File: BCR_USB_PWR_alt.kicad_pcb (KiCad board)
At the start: 2 copper layers, 32.2 x 17 mm, 2 parts, among them CN1 DB9_Female, CN2 UE27AC54100

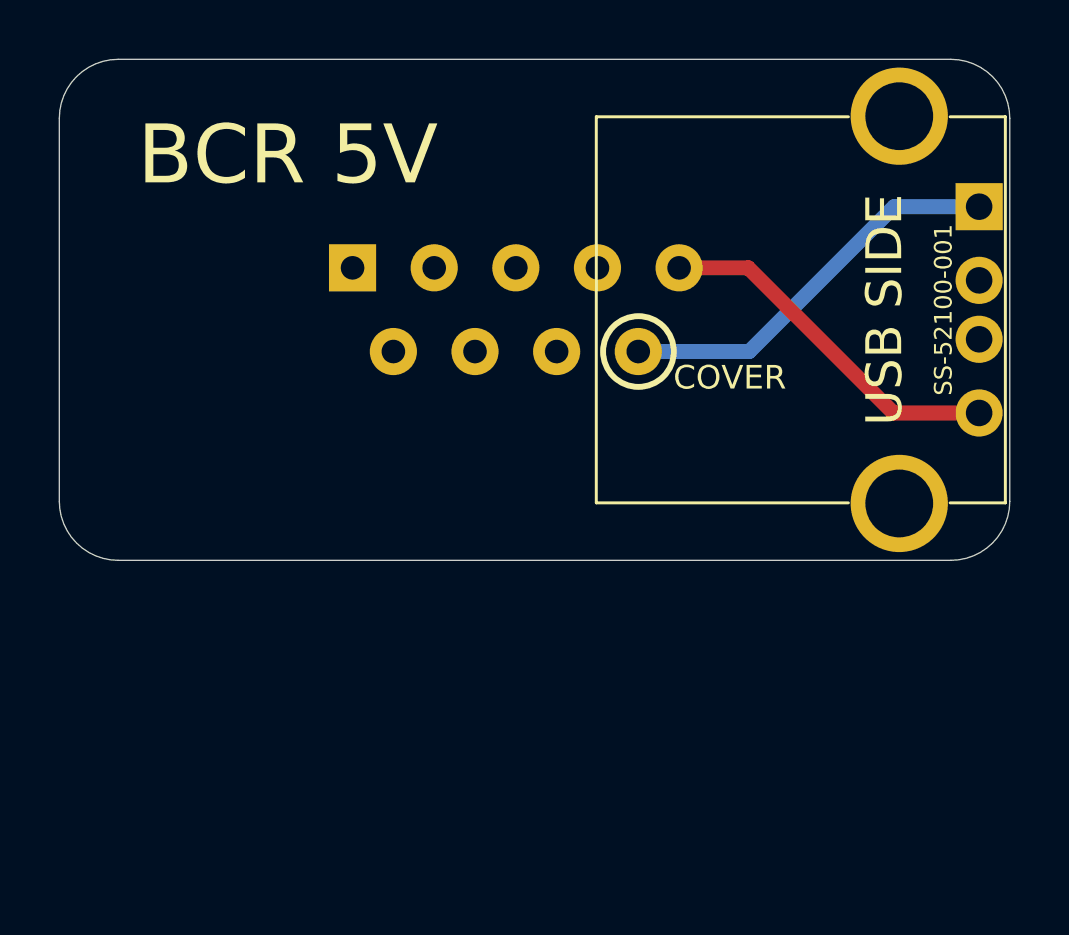
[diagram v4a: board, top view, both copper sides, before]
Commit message: db9 pin 7 is the real GND, not pin 5
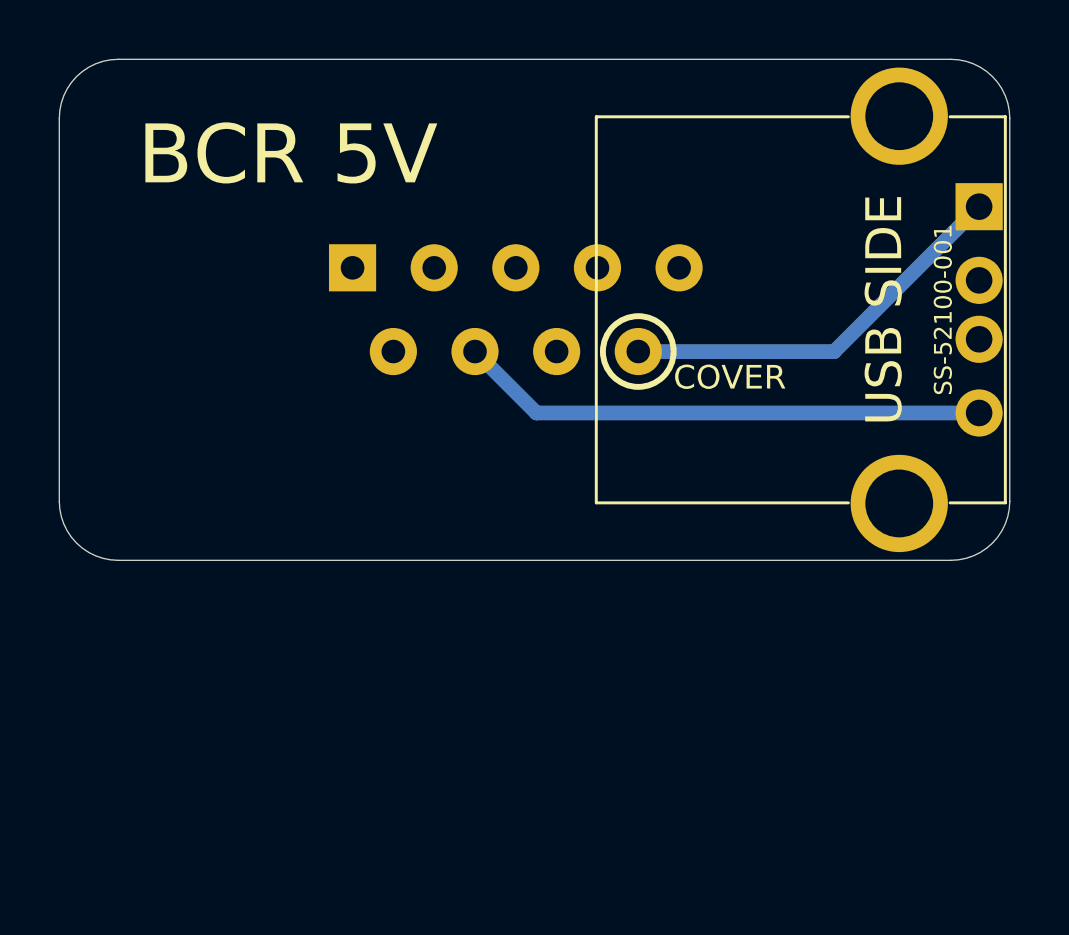
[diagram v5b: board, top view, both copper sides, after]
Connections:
- CN1 pad 5: /GND -> (no net)
- CN1 pad 7: (no net) -> /GND
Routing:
- net /GND: track 12.2 -> 18.0 mm
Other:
- net class Default: clearance 0.2 -> 0.16; trace_width 0.25 -> 0.16; via_dia 0.8 -> 0.42; via_drill 0.4 -> 0.26
- rule trace_clearance: 0.2 -> 0.16
- rule trace_min: 0.2 -> 0.16
- rule via_min_drill: 0.3 -> 0.26
- rule via_min_size: 0.4 -> 0.42
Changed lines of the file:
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@@
     (thickness 1.6)
     (drawings 23)
-    (tracks 6)
+    (tracks 4)
     (zones 0)
     (modules 2)
@@
   )
   (setup
-    (last_trace_width 0.25)
-    (user_trace_width 0.508)
-    (trace_clearance 0.2)
+    (last_trace_width 0.16)
+    (user_trace_width 0.5)
+    (trace_clearance 0.16)
     (zone_clearance 0.508)
     (zone_45_only no)
-    (trace_min 0.2)
-    (via_size 0.8)
-    (via_drill 0.4)
-    (via_min_size 0.4)
-    (via_min_drill 0.3)
-    (user_via 0.508 0.3048)
+    (trace_min 0.16)
+    (via_size 0.42)
+    (via_drill 0.26)
+    (via_min_size 0.42)
+    (via_min_drill 0.26)
     (uvia_size 0.3)
     (uvia_drill 0.1)
@@
     (mod_text_size 1 1)
     (mod_text_width 0.15)
-    (pad_size 1.524 1.524)
-    (pad_drill 0.762)
+    (pad_size 1.6 1.6)
+    (pad_drill 0.8)
     (pad_to_mask_clearance 0)
     (aux_axis_origin 0 0)
@@
   (net 3 "Net-(CN2-PadSH)")
   (net_class Default "This is the default net class."
-    (clearance 0.2)
-    (trace_width 0.25)
-    (via_dia 0.8)
-    (via_drill 0.4)
+    (clearance 0.16)
+    (trace_width 0.16)
+    (via_dia 0.42)
+    (via_drill 0.26)
     (uvia_dia 0.3)
     (uvia_drill 0.1)
@@
       (net 1 /+5V))
     (pad 8 thru_hole circle (at -6.925 -2.84 180) (size 1.6 1.6) (drill 0.8) (layers *.Cu *.Mask))
-    (pad 7 thru_hole circle (at -4.155 -2.84 180) (size 1.6 1.6) (drill 0.8) (layers *.Cu *.Mask))
+    (pad 7 thru_hole circle (at -4.155 -2.84 180) (size 1.6 1.6) (drill 0.8) (layers *.Cu *.Mask)
+      (net 2 /GND))
     (pad 6 thru_hole circle (at -1.385 -2.84 180) (size 1.6 1.6) (drill 0.8) (layers *.Cu *.Mask))
-    (pad 5 thru_hole circle (at -11.08 0 180) (size 1.6 1.6) (drill 0.8) (layers *.Cu *.Mask)
-      (net 2 /GND))
+    (pad 5 thru_hole circle (at -11.08 0 180) (size 1.6 1.6) (drill 0.8) (layers *.Cu *.Mask))
     (pad 4 thru_hole circle (at -8.31 0 180) (size 1.6 1.6) (drill 0.8) (layers *.Cu *.Mask))
     (pad 3 thru_hole circle (at -5.54 0 180) (size 1.6 1.6) (drill 0.8) (layers *.Cu *.Mask))
@@
     (effects (font (size 0.8 0.8) (thickness 0.1)))
   )
-  (gr_circle (center 131.15 97.173) (end 132.35 97.173) (layer F.SilkS) (width 0.2))
+  (gr_circle (center 131.145 97.173) (end 132.345 97.173) (layer F.SilkS) (width 0.2))
   (gr_line (start 120.65 93.533) (end 120.65 97.983) (layer Dwgs.User) (width 0.15))
   (gr_line (start 133.35 93.533) (end 120.65 93.533) (layer Dwgs.User) (width 0.15))
@@
   (gr_line (start 143.75 102.258) (end 143.75 89.258) (layer Edge.Cuts) (width 0.0254))
   (gr_line (start 113.5 104.258) (end 141.75 104.258) (layer Edge.Cuts) (width 0.0254))
-  (segment (start 134.91 97.173) (end 131.145 97.173) (width 0.508) (layer B.Cu) (net 1))
-  (segment (start 142.71 92.258) (end 139.825 92.258) (width 0.508) (layer B.Cu) (net 1))
-  (segment (start 139.825 92.258) (end 134.91 97.173) (width 0.508) (layer B.Cu) (net 1))
-  (segment (start 134.875 94.333) (end 132.53 94.333) (width 0.508) (layer F.Cu) (net 2))
-  (segment (start 142.71 99.258) (end 139.8 99.258) (width 0.508) (layer F.Cu) (net 2))
-  (segment (start 139.8 99.258) (end 134.875 94.333) (width 0.508) (layer F.Cu) (net 2))
+  (segment (start 137.795 97.173) (end 142.71 92.258) (width 0.5) (layer B.Cu) (net 1))
+  (segment (start 131.145 97.173) (end 137.795 97.173) (width 0.5) (layer B.Cu) (net 1))
+  (segment (start 127.69 99.258) (end 142.71 99.258) (width 0.5) (layer B.Cu) (net 2))
+  (segment (start 125.605 97.173) (end 127.69 99.258) (width 0.5) (layer B.Cu) (net 2))
 )
